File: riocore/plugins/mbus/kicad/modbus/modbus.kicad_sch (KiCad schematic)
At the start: 6 parts, among them U12 MAX485E

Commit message: kicad: module selection / some fixes
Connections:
- net rw renamed tx_enable
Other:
- moved on the sheet: C3
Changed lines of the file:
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@@
 	(global_label "3v3"
 		(shape input)
-		(at 107.95 92.71 90)
+		(at 100.33 95.25 90)
 		(fields_autoplaced yes)
 		(effects
@@
 		)
 		(property "Intersheetrefs" "${INTERSHEET_REFS}"
-			(at 107.95 86.4176 90)
+			(at 100.33 88.9576 90)
 			(effects
 				(font
@@
 	(global_label "gnd"
 		(shape input)
-		(at 107.95 100.33 270)
-		(fields_autoplaced yes)
-		(effects
-			(font
-				(size 1.27 1.27)
-			)
-			(justify right)
-		)
-		(property "Intersheetrefs" "${INTERSHEET_REFS}"
-			(at 107.95 106.6828 90)
+		(at 100.33 102.87 270)
+		(fields_autoplaced yes)
+		(effects
+			(font
+				(size 1.27 1.27)
+			)
+			(justify right)
+		)
+		(property "Intersheetrefs" "${INTERSHEET_REFS}"
+			(at 100.33 109.2228 90)
 			(effects
 				(font
@@
 		)
 	)
-	(hierarchical_label "rw"
+	(hierarchical_label "tx_enable"
 		(shape input)
 		(at 121.92 96.52 180)
@@
 	(symbol
 		(lib_id "Device:C")
-		(at 107.95 96.52 0)
+		(at 100.33 99.06 0)
 		(unit 1)
 		(exclude_from_sim no)
@@
 		(fields_autoplaced yes)
 		(property "Reference" "C3"
-			(at 111.76 95.25 0)
+			(at 104.14 97.79 0)
 			(effects
 				(font
@@
 		)
 		(property "Value" "100n"
-			(at 111.76 97.79 0)
+			(at 104.14 100.33 0)
 			(effects
 				(font
@@
 		)
 		(property "Footprint" "Capacitor_SMD:C_1206_3216Metric"
-			(at 108.9152 100.33 0)
+			(at 101.2952 102.87 0)
 			(effects
 				(font
@@
 		)
 		(property "Datasheet" "~"
-			(at 107.95 96.52 0)
+			(at 100.33 99.06 0)
 			(effects
 				(font
@@
 		)
 		(property "Description" ""
-			(at 107.95 96.52 0)
-			(effects
-				(font
+			(at 100.33 99.06 0)
+			(effects
+				(font

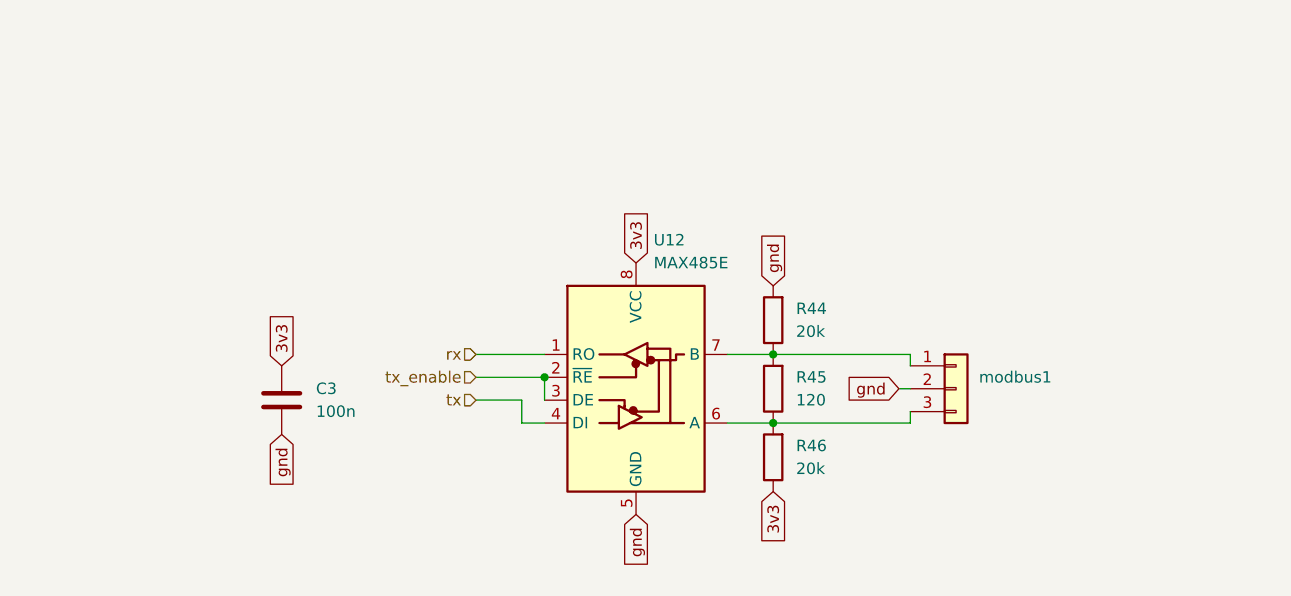
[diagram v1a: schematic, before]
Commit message: modbus: kicad: iso
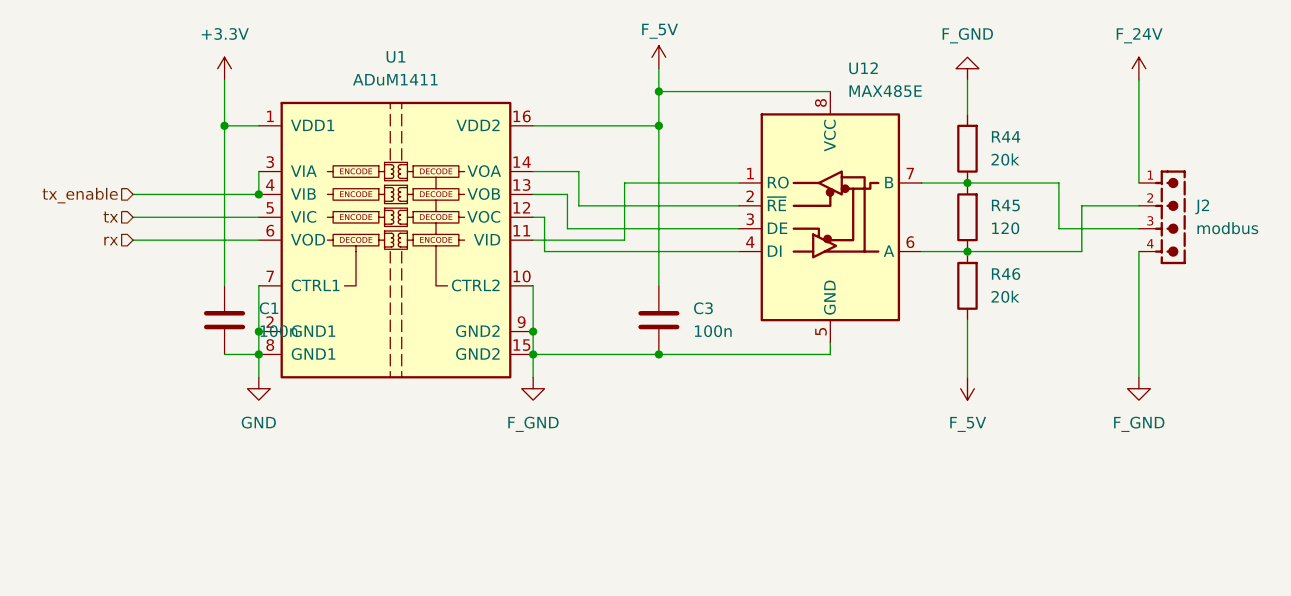
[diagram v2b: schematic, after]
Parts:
- removed modbus1: Conn_01x03, Connector_JST:JST_XH_B3B-XH-A_1x03_P2.50mm_Vertical, symbol Connector_Generic:Conn_01x03
- added C1: 100n, Capacitor_SMD:C_1206_3216Metric, symbol Device:C
- added J2: modbus, kicad-lbr:691322110004, symbol 691322110004:691322110004
- added U1: ADuM1411, Package_SO:SOIC-16W_7.5x10.3mm_P1.27mm, symbol Isolator:ADuM1411
- U12: footprint Package_SO:Diodes_SO-8EP -> Package_SO:SOIC-8_3.9x4.9mm_P1.27mm
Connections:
- net rx: now also U1.6 (VOD); no longer U12.1 (RO)
- net tx: now also U1.5 (VIC); no longer U12.4 (DI)
- net tx_enable: now also U1.3 (VIA), U1.4 (VIB); no longer U12.2 (~{RE}), U12.3 (DE)
- net at R45.1, R46.2, U12.6 (A): now also J2.2
- net at R44.1, R45.2, U12.7 (B): now also J2.3
- net 3v3 renamed F_5V
- net F_5V: now also U1.16 (VDD2)
- net gnd renamed F_GND
- net F_GND: now also J2.4, U1.10 (CTRL2), U1.15 (GND2), U1.9 (GND2)
- new net: U1.11 (VID), U12.1 (RO)
- new net: U1.14 (VOA), U12.2 (~{RE})
- new net: U1.13 (VOB), U12.3 (DE)
- new net: U1.12 (VOC), U12.4 (DI)
- new net +3.3V: C1.1, U1.1 (VDD1)
- new net F_24V: J2.1
- new net GND: C1.2, U1.2 (GND1), U1.7 (CTRL1), U1.8 (GND1)
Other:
- moved on the sheet: C3, R44, R45, R46, U12
